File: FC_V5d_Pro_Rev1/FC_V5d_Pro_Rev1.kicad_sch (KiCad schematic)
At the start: 80 parts, among them IC3 RV-3028-C7_32.768kHz_1ppm_TA_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, J1 Conn_01x02, J12 USB_C_Receptacle_USB2.0_16P, J16 DEBUG, J18 Payload, J22 SWD Port, J3 Life Makes Lemonade, J5 BM04B-SRSS-TB(LF)(SN), SW1 KMR2, SW2 KMR2, U12 TCA9548ARGERQ1, U14 TCA4307DGKR, U15 LIS2MDL, U2 ZDSD04GLGEAG, U30 E28-2G4M27S, U4 RFM98PW, U7 LSM6DSOTR

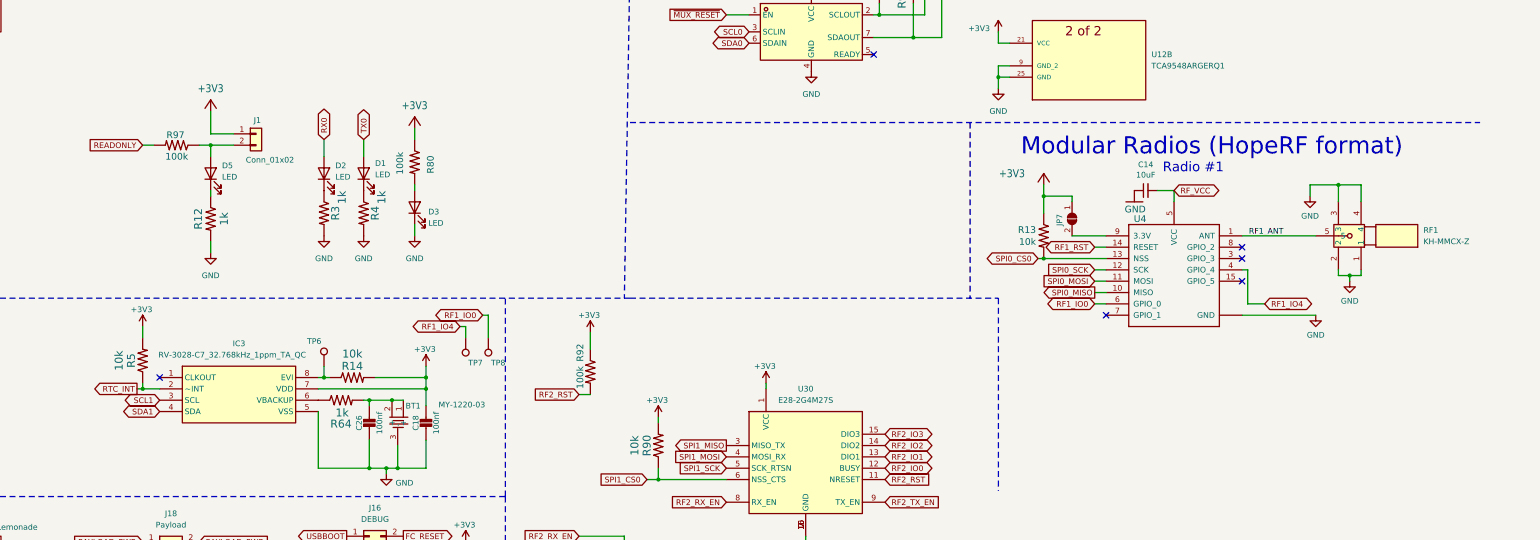
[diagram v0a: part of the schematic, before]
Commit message: Updated to add 5V_RESET Line
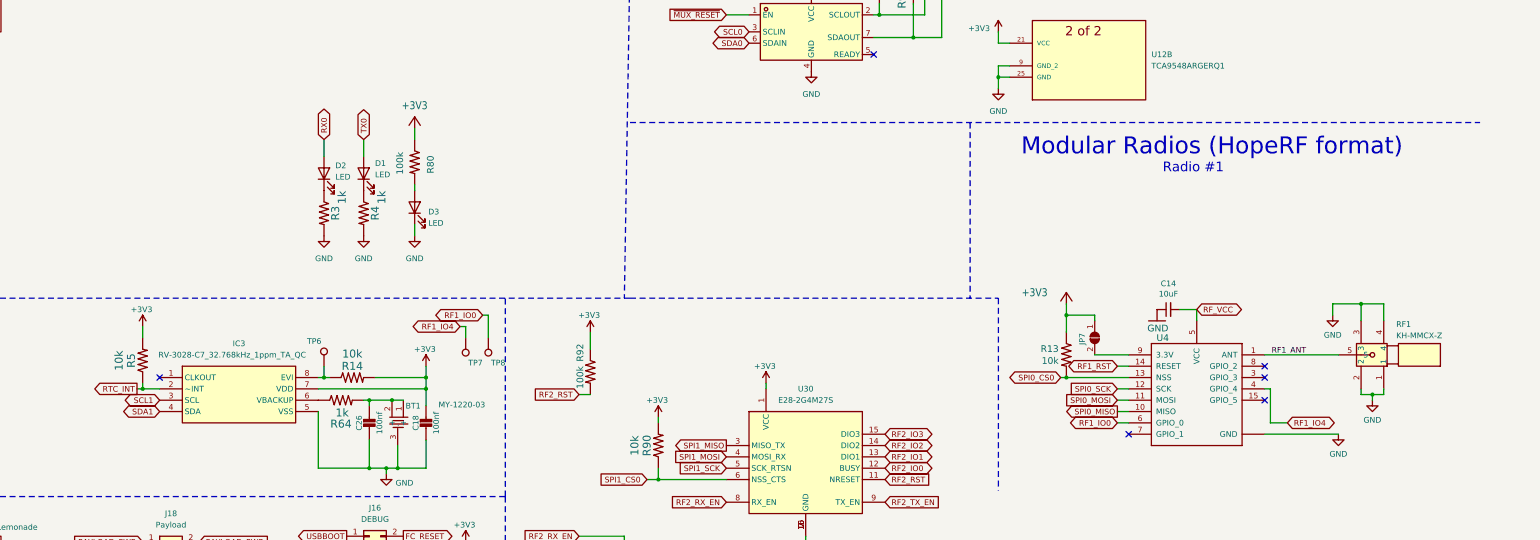
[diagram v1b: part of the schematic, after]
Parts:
- removed D5: LED, LED_SMD:LED_0603_1608Metric, symbol Device:LED
- removed J1: Conn_01x02, Connector_PinHeader_2.54mm:PinHeader_1x02_P2.54mm_Vertical, symbol Connector_Generic:Conn_01x02
- removed R12: 1k, Resistor_SMD:R_0603_1608Metric, symbol mainboard:RESISTOR0603
- removed R97: 100k, Resistor_SMD:R_0603_1608Metric, symbol mainboard:R-US_R0603
- R44, R53, R56: footprint Resistor_SMD:R_0603_1608Metric -> Resistor_SMD:R_0402_1005Metric
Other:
- moved on the sheet: C14, JP7, R13, RF1, U4

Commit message: V5dpR1 As Ordered Nov 12, 2025
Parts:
- added C11: 100uF, Capacitor_SMD:C_1210_3225Metric, symbol mainboard:22UF-1210-16V-20%
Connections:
- net GND: now also C11.1
- net RF_VCC: now also C11.2
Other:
- moved on the sheet: C14
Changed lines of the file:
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@@
 	)
 	(junction
+		(at 344.17 212.09)
+		(diameter 0)
+		(color 0 0 0 0)
+	)
+	(junction
 		(at 165.1 247.65)
 		(diameter 0)
@@
 	)
 	(junction
+		(at 335.28 212.09)
+		(diameter 0)
+		(color 0 0 0 0)
+	)
+	(junction
 		(at 163.83 232.41)
 		(diameter 0)
@@
 	(wire
 		(pts
+			(xy 335.28 203.2) (xy 335.28 212.09)
+		)
+		(stroke
+			(width 0)
+			(type default)
+		)
+	)
+	(wire
+		(pts
 			(xy 368.3 114.3) (xy 368.3 123.19)
 		)
@@
 	(wire
 		(pts
+			(xy 344.17 203.2) (xy 342.9 203.2)
+		)
+		(stroke
+			(width 0)
+			(type default)
+		)
+	)
+	(wire
+		(pts
 			(xy 148.59 227.33) (xy 149.86 227.33)
 		)
@@
 	(wire
 		(pts
-			(xy 344.17 212.09) (xy 340.36 212.09)
+			(xy 344.17 212.09) (xy 341.63 212.09)
 		)
 		(stroke
@@
 	(wire
 		(pts
+			(xy 336.55 212.09) (xy 335.28 212.09)
+		)
+		(stroke
+			(width 0)
+			(type default)
+		)
+	)
+	(wire
+		(pts
 			(xy 106.68 229.87) (xy 107.95 229.87)
 		)
@@
 	(wire
 		(pts
+			(xy 344.17 212.09) (xy 344.17 203.2)
+		)
+		(stroke
+			(width 0)
+			(type default)
+		)
+	)
+	(wire
+		(pts
 			(xy 280.67 132.08) (xy 276.86 132.08)
 		)
@@
 	(symbol
 		(lib_id "Device:C_Small")
-		(at 337.82 212.09 90)
+		(at 339.09 212.09 90)
 		(unit 1)
 		(exclude_from_sim no)
@@
 		(dnp no)
 		(property "Reference" "C14"
-			(at 337.82 206.2734 90)
+			(at 339.09 206.2734 90)
 			(effects
 				(font
@@
 		)
 		(property "Value" "10uF"
-			(at 337.82 208.5848 90)
+			(at 339.09 208.5848 90)
 			(effects
 				(font
@@
 		)
 		(property "Footprint" "Capacitor_SMD:C_0603_1608Metric"
-			(at 337.82 212.09 0)
+			(at 339.09 212.09 0)
 			(effects
 				(font
@@
 		)
 		(property "Datasheet" "~"
-			(at 337.82 212.09 0)
+			(at 339.09 212.09 0)
 			(effects
 				(font
@@
 		)
 		(property "Description" "10uF +-20% 10V X5R"
-			(at 337.82 212.09 0)
+			(at 339.09 212.09 0)
 			(effects
 				(font
@@
 					(unit 1)
 				)
+			)
+		)
+	)
+	(symbol
+		(lib_id "mainboard:22UF-1210-16V-20%")
+		(at 340.36 203.2 90)
+		(unit 1)
+		(exclude_from_sim no)
+		(in_bom yes)
+		(on_board yes)
+		(dnp no)
+		(property "Reference" "C11"
+			(at 339.09 200.66 0)
+			(effects
+				(font
+					(size 1.778 1.778)
+				)
+				(justify left bottom)
+			)
+		)
+		(property "Value" "100uF"
+			(at 342.519 201.676 0)
+			(effects
+				(font
+					(size 1.778 1.778)
+				)
+				(justify left bottom)
+			)
+		)
+		(property "Footprint" "Capacitor_SMD:C_1210_3225Metric"
+			(at 340.36 203.2 0)
+			(effects
+				(font
+					(size 1.27 1.27)
+				)
+				(hide yes)
+			)
+		)
+		(property "Datasheet" ""
+			(at 340.36 203.2 0)
+			(effects
+				(font
+					(size 1.27 1.27)
+				)
+				(hide yes)
+			)
+		)
+		(property "Description" "100uF 16V X5R 1210"
+			(at 340.36 203.2 0)
+			(effects
+				(font
+					(size 1.27 1.27)
+				)
+				(hide yes)
+			)
+		)
+		(pin "1"
+		)
+		(pin "2"
+		)
+		(instances
+			(project "FC_V5d_Pro_Rev1"
+				(path "/c64c0d72-a9f6-4f3a-891e-1f647558f538"
+					(reference "C11")
+					(unit 1)
+				)
